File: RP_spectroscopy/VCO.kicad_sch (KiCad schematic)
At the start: 5 parts, among them IC1 TL081CDR, IC2 TL081CDR, IC3 TL081CDR, U11 TL431LPG, U7 INA114BU

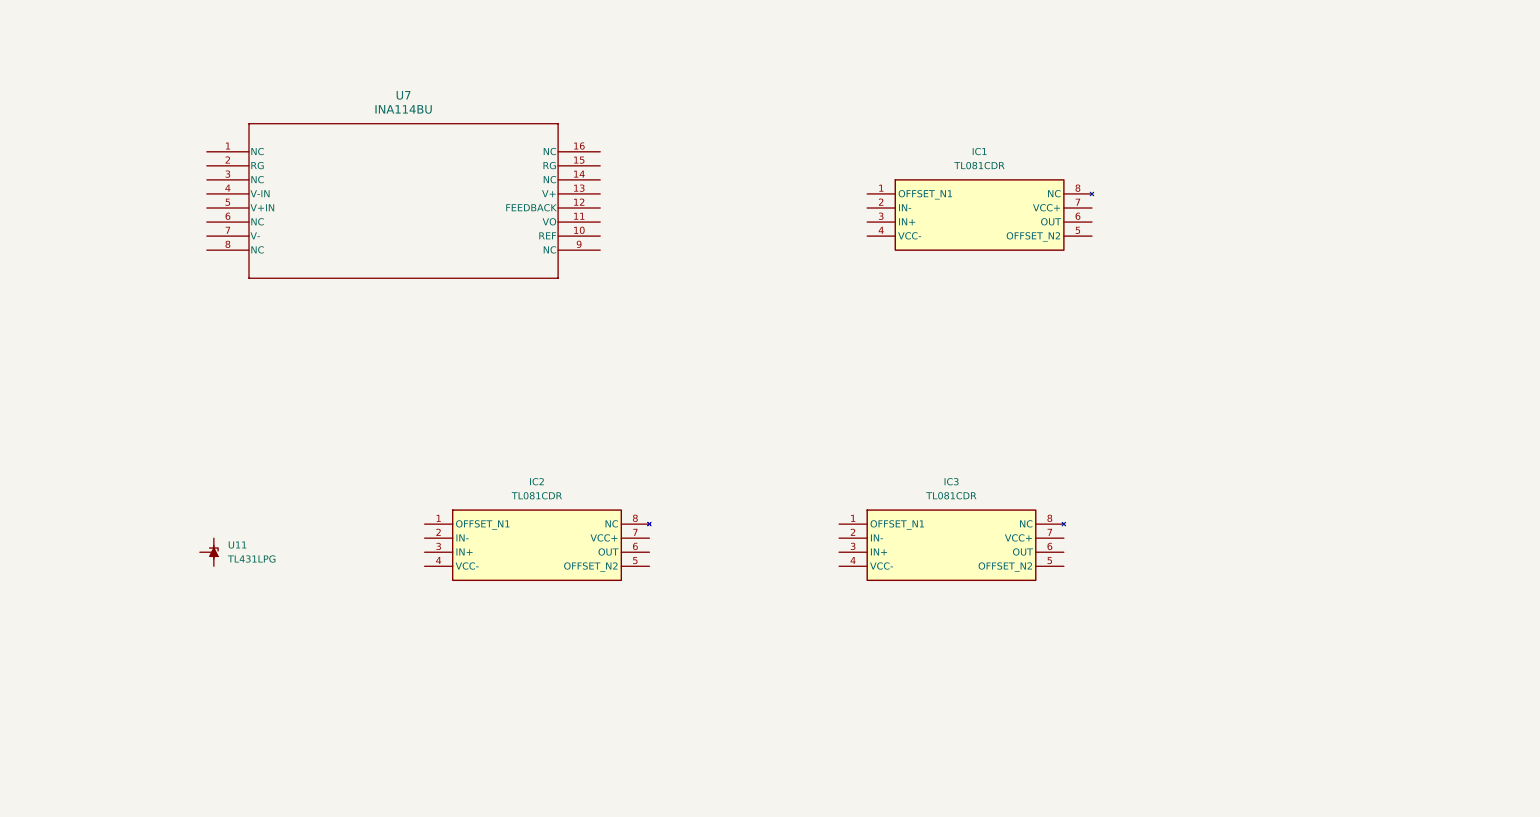
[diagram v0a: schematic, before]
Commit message: Implemented almost completely the VCO, apart from the VCO component itself
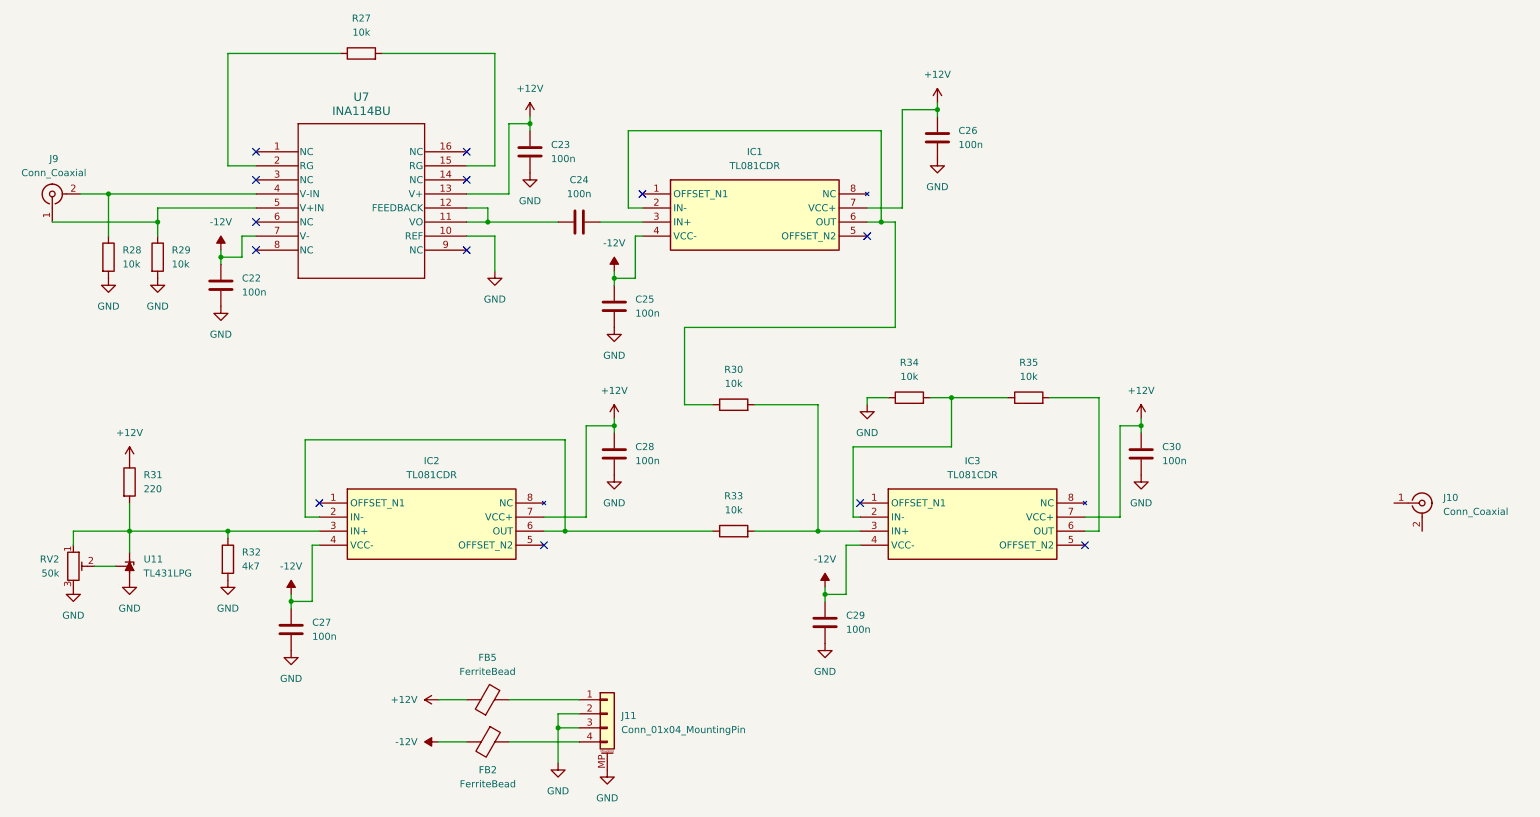
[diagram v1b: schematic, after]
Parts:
- added C22, C23, C24, C25, C26, C27, C28, C29, C30: 100n, symbol Device:C
- added FB2, FB5: FerriteBead, symbol Device:FerriteBead
- added J10, J9: Conn_Coaxial, Connector_Coaxial:SMA_Molex_73251-1153_EdgeMount_Horizontal, symbol Connector:Conn_Coaxial
- added J11: Conn_01x04_MountingPin, Connector_Molex:Molex_PicoBlade_53261-0471_1x04-1MP_P1.25mm_Horizontal, symbol Connector_Generic_MountingPin:Conn_01x04_MountingPin
- added R27, R28, R29, R30, R33, R34, R35: 10k, symbol Device:R
- added R31: 220, symbol Device:R
- added R32: 4k7, symbol Device:R
- added RV2: 50k, symbol Device:R_Potentiometer_Trim
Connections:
- net at IC2.2 (IN-): now also IC2.6 (OUT), R33.1
- net at IC2.3 (IN+): now also U11.3 (K), R31.2, R32.1, RV2.1
- net -12V: now reaches IC2.4 (VCC-)
- net -12V: now also IC1.4 (VCC-), IC3.4 (VCC-), U7.7 (V-), C22.1, C25.1, C27.1, C29.1, FB2.2
- net +12V: now reaches IC2.7 (VCC+)
- net +12V: now also IC1.7 (VCC+), IC3.7 (VCC+), U7.13 (V+), C23.1, C26.1, C28.1, C30.1, FB5.1, R31.1
- net at U11.1 (REF): now also RV2.2
- net GND: now reaches U11.2 (A)
- net GND: now also U7.10 (REF), C22.2, C23.2, C25.2, C26.2, C27.2, C28.2, C29.2, C30.2, J11.2 (Pin_2), J11.3 (Pin_3), J11.MP (MountPin), R28.2, R29.2, R32.2, R34.1, RV2.3
- net at IC1.2 (IN-): now also IC1.6 (OUT), R30.1
- net at IC1.3 (IN+): now also C24.2
- net at IC3.2 (IN-): now also R34.2, R35.1
- net at IC3.3 (IN+): now also R30.2, R33.2
- net at IC3.6 (OUT): now also R35.2
- net at U7.11 (VO): now also U7.12 (FEEDBACK), C24.1
- net at U7.15 (RG): now also R27.2
- net at U7.2 (RG): now also R27.1
- net at U7.4 (V-IN): now also J9.2 (Ext), R28.1
- net at U7.5 (V+IN): now also J9.1 (In), R29.1
- new net: FB2.1, J11.4 (Pin_4)
- new net: FB5.2, J11.1 (Pin_1)
- no-connect marks 0 -> 13
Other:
- moved on the sheet: IC1, IC2, IC3, U11, U7

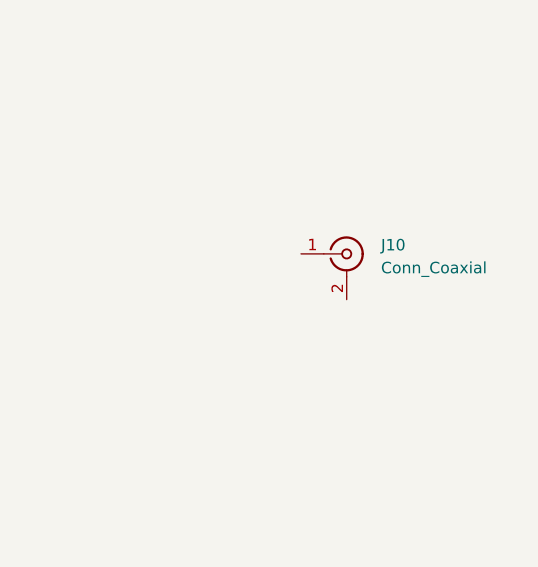
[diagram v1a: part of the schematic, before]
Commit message: Commit before deleting the VCO schematic from the main project. I have a separate project for that.
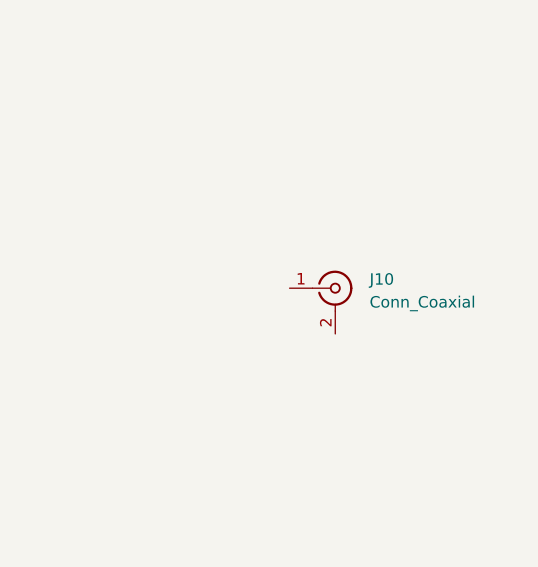
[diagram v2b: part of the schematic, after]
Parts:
- C22, C23, C24, C25, C26, C27, C28, C29, C30: footprint (none) -> Capacitor_SMD:C_0805_2012Metric_Pad1.18x1.45mm_HandSolder
- FB2, FB5: footprint (none) -> Ferrite_THT:FerriteBread
- R27, R28, R29, R30, R31, R32, R33, R34, R35: footprint (none) -> Resistor_SMD:R_0805_2012Metric_Pad1.20x1.40mm_HandSolder
- RV2: footprint (none) -> Potentiometer_THT:Potentiometer_Runtron_RM-063_Horizontal
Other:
- moved on the sheet: J10
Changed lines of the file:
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@@
 			)
 		)
-		(property "Footprint" ""
+		(property "Footprint" "Potentiometer_THT:Potentiometer_Runtron_RM-063_Horizontal"
 			(at 22.86 133.35 0)
 			(effects
@@
 			)
 		)
-		(property "Footprint" ""
+		(property "Footprint" "Resistor_SMD:R_0805_2012Metric_Pad1.20x1.40mm_HandSolder"
 			(at 195.58 104.648 90)
 			(effects
@@
 			)
 		)
-		(property "Description" "Resistor"
+		(property "Description" "Resistor, 10k 1%"
 			(at 195.58 102.87 0)
 			(effects
@@
 			)
 		)
-		(property "Description" "coaxial connector (BNC, SMA, SMB, SMC, Cinch/RCA, LEMO, ...)"
+		(property "Description" "SMA RF connector, edge mount"
 			(at 19.05 66.04 0)
 			(effects
@@
 			)
 		)
-		(property "Footprint" ""
+		(property "Footprint" "Resistor_SMD:R_0805_2012Metric_Pad1.20x1.40mm_HandSolder"
 			(at 27.432 77.47 90)
 			(effects
@@
 			)
 		)
-		(property "Description" "Resistor"
+		(property "Description" "Resistor, 10k 1%"
 			(at 29.21 77.47 0)
 			(effects
@@
 			)
 		)
-		(property "Footprint" ""
+		(property "Footprint" "Resistor_SMD:R_0805_2012Metric_Pad1.20x1.40mm_HandSolder"
 			(at 74.93 42.418 90)
 			(effects
@@
 			)
 		)
-		(property "Description" "Resistor"
+		(property "Description" "Resistor, 10k 1%"
 			(at 74.93 40.64 0)
 			(effects
@@
 			)
 		)
-		(property "Footprint" ""
+		(property "Footprint" "Capacitor_SMD:C_0805_2012Metric_Pad1.18x1.45mm_HandSolder"
 			(at 106.3752 62.23 0)
 			(effects
@@
 			)
 		)
-		(property "Description" "Unpolarized capacitor"
+		(property "Description" "Unpolarized capacitor, 100n X7R 50V"
 			(at 105.41 58.42 0)
 			(effects
@@
 			)
 		)
-		(property "Footprint" ""
+		(property "Footprint" "Capacitor_SMD:C_0805_2012Metric_Pad1.18x1.45mm_HandSolder"
 			(at 121.6152 90.17 0)
 			(effects
@@
 			)
 		)
-		(property "Description" "Unpolarized capacitor"
+		(property "Description" "Unpolarized capacitor, 100n X7R 50V"
 			(at 120.65 86.36 0)
 			(effects
@@
 			)
 		)
-		(property "Footprint" ""
+		(property "Footprint" "Resistor_SMD:R_0805_2012Metric_Pad1.20x1.40mm_HandSolder"
 			(at 142.24 105.918 90)
 			(effects
@@
 			)
 		)
-		(property "Description" "Resistor"
+		(property "Description" "Resistor, 10k 1%"
 			(at 142.24 104.14 0)
 			(effects
@@
 			)
 		)
-		(property "Footprint" ""
+		(property "Footprint" "Capacitor_SMD:C_0805_2012Metric_Pad1.18x1.45mm_HandSolder"
 			(at 121.6152 116.84 0)
 			(effects
@@
 			)
 		)
-		(property "Description" "Unpolarized capacitor"
+		(property "Description" "Unpolarized capacitor, 100n X7R 50V"
 			(at 120.65 113.03 0)
 			(effects
@@
 			)
 		)
-		(property "Footprint" ""
+		(property "Footprint" "Resistor_SMD:R_0805_2012Metric_Pad1.20x1.40mm_HandSolder"
 			(at 142.24 128.778 90)
 			(effects
@@
 			)
 		)
-		(property "Description" "Resistor"
+		(property "Description" "Resistor, 10k 1%"
 			(at 142.24 127 0)
 			(effects
@@
 			)
 		)
-		(property "Footprint" ""
+		(property "Footprint" "Resistor_SMD:R_0805_2012Metric_Pad1.20x1.40mm_HandSolder"
 			(at 36.322 77.47 90)
 			(effects
@@
 			)
 		)
-		(property "Description" "Resistor"
+		(property "Description" "Resistor, 10k 1%"
 			(at 38.1 77.47 0)
 			(effects
@@
 			)
 		)
-		(property "Footprint" ""
+		(property "Footprint" "Ferrite_THT:FerriteBread"
 			(at 97.79 163.322 90)
 			(effects
@@
 			)
 		)
-		(property "Footprint" ""
+		(property "Footprint" "Resistor_SMD:R_0805_2012Metric_Pad1.20x1.40mm_HandSolder"
 			(at 173.99 104.648 90)
 			(effects
@@
 			)
 		)
-		(property "Description" "Resistor"
+		(property "Description" "Resistor, 10k 1%"
 			(at 173.99 102.87 0)
 			(effects
@@
 			)
 		)
-		(property "Footprint" ""
+		(property "Footprint" "Capacitor_SMD:C_0805_2012Metric_Pad1.18x1.45mm_HandSolder"
 			(at 180.0352 59.69 0)
 			(effects
@@
 			)
 		)
-		(property "Description" "Unpolarized capacitor"
+		(property "Description" "Unpolarized capacitor, 100n X7R 50V"
 			(at 179.07 55.88 0)
 			(effects
@@
 			)
 		)
-		(property "Footprint" ""
+		(property "Footprint" "Capacitor_SMD:C_0805_2012Metric_Pad1.18x1.45mm_HandSolder"
 			(at 118.11 70.1548 0)
 			(effects
@@
 			)
 		)
-		(property "Description" "Unpolarized capacitor"
+		(property "Description" "Unpolarized capacitor, 100n X7R 50V"
 			(at 114.3 71.12 0)
 			(effects
@@
 			)
 		)
-		(property "Footprint" ""
+		(property "Footprint" "Capacitor_SMD:C_0805_2012Metric_Pad1.18x1.45mm_HandSolder"
 			(at 63.1952 148.59 0)
 			(effects
@@
 			)
 		)
-		(property "Description" "Unpolarized capacitor"
+		(property "Description" "Unpolarized capacitor, 100n X7R 50V"
 			(at 62.23 144.78 0)
 			(effects
@@
 			)
 		)
-		(property "Footprint" ""
+		(property "Footprint" "Resistor_SMD:R_0805_2012Metric_Pad1.20x1.40mm_HandSolder"
 			(at 31.242 118.11 90)
 			(effects
@@
 			)
 		)
-		(property "Description" "Resistor"
+		(property "Description" "Resistor, 220R 1%"
 			(at 33.02 118.11 0)
 			(effects
@@
 			)
 		)
-		(property "Footprint" ""
+		(property "Footprint" "Capacitor_SMD:C_0805_2012Metric_Pad1.18x1.45mm_HandSolder"
 			(at 216.8652 116.84 0)
 			(effects
@@
 			)
 		)
-		(property "Description" "Unpolarized capacitor"
+		(property "Description" "Unpolarized capacitor, 100n X7R 50V"
 			(at 215.9 113.03 0)
 			(effects
@@
 	(symbol
 		(lib_id "Connector:Conn_Coaxial")
-		(at 266.7 121.92 0)
+		(at 265.43 125.73 0)
 		(unit 1)
 		(exclude_from_sim no)
@@
 		(fields_autoplaced yes)
 		(property "Reference" "J10"
-			(at 270.51 120.9431 0)
+			(at 269.24 124.7531 0)
 			(effects
 				(font
@@
 		)
 		(property "Value" "Conn_Coaxial"
-			(at 270.51 123.4831 0)
+			(at 269.24 127.2931 0)
 			(effects
 				(font
@@
 		)
 		(property "Footprint" "Connector_Coaxial:SMA_Molex_73251-1153_EdgeMount_Horizontal"
-			(at 266.7 121.92 0)
+			(at 265.43 125.73 0)
 			(effects
 				(font
@@
 		)
 		(property "Datasheet" "~"
-			(at 266.7 121.92 0)
+			(at 265.43 125.73 0)
 			(effects
 				(font
@@
 			)
 		)
-		(property "Description" "coaxial connector (BNC, SMA, SMB, SMC, Cinch/RCA, LEMO, ...)"
-			(at 266.7 121.92 0)
+		(property "Description" "SMA RF connector, edge mount"
+			(at 265.43 125.73 0)
 			(effects
 				(font
@@
 			)
 		)
-		(property "Footprint" ""
+		(property "Footprint" "Capacitor_SMD:C_0805_2012Metric_Pad1.18x1.45mm_HandSolder"
 			(at 50.4952 86.36 0)
 			(effects
@@
 			)
 		)
-		(property "Description" "Unpolarized capacitor"
+		(property "Description" "Unpolarized capacitor, 100n X7R 50V"
 			(at 49.53 82.55 0)
 			(effects
@@
 			)
 		)
-		(property "Footprint" ""
+		(property "Footprint" "Ferrite_THT:FerriteBread"
 			(at 97.79 159.258 90)
 			(effects
@@
 			)
 		)
-		(property "Footprint" ""
+		(property "Footprint" "Resistor_SMD:R_0805_2012Metric_Pad1.20x1.40mm_HandSolder"
 			(at 49.022 132.08 90)
 			(effects
@@
 			)
 		)
-		(property "Description" "Resistor"
+		(property "Description" "Resistor, 4k7 1%"
 			(at 50.8 132.08 0)
 			(effects
@@
 			)
 		)
-		(property "Footprint" ""
+		(property "Footprint" "Capacitor_SMD:C_0805_2012Metric_Pad1.18x1.45mm_HandSolder"
 			(at 159.7152 147.32 0)
 			(effects
@@
 			)
 		)
-		(property "Description" "Unpolarized capacitor"
+		(property "Description" "Unpolarized capacitor, 100n X7R 50V"
 			(at 158.75 143.51 0)
 			(effects
